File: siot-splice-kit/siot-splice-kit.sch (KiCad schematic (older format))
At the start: 2 parts, among them J1 xConnect_smd, J2 Screw_Terminal_5mm_01x03

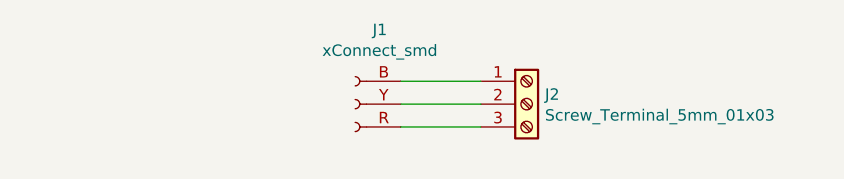
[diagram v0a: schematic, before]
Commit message: updates for relay/splice kit
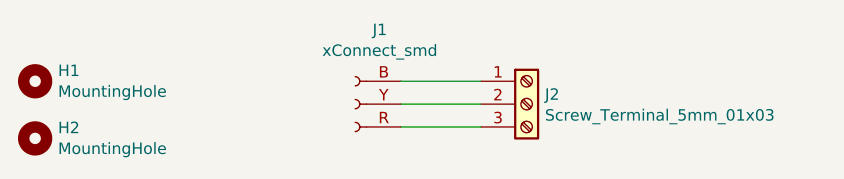
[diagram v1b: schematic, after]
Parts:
- added H1, H2: MountingHole, MountingHole:MountingHole_3.5mm, symbol Mechanical:MountingHole
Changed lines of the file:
@@
 EESchema Schematic File Version 4
+LIBS:siot-splice-kit-cache
 EELAYER 30 0
 EELAYER END
@@
 Wire Wire Line
 	4100 3350 4450 3350
+$Comp
+L Mechanical:MountingHole H1
+U 1 1 5DB9C90A
+P 2500 3150
+F 0 "H1" H 2600 3196 50  0000 L CNN
+F 1 "MountingHole" H 2600 3105 50  0000 L CNN
+F 2 "MountingHole:MountingHole_3.5mm" H 2500 3150 50  0001 C CNN
+F 3 "~" H 2500 3150 50  0001 C CNN
+	1    2500 3150
+	1    0    0    -1
+$EndComp
+$Comp
+L Mechanical:MountingHole H2
+U 1 1 5DB9C910
+P 2500 3400
+F 0 "H2" H 2600 3446 50  0000 L CNN
+F 1 "MountingHole" H 2600 3355 50  0000 L CNN
+F 2 "MountingHole:MountingHole_3.5mm" H 2500 3400 50  0001 C CNN
+F 3 "~" H 2500 3400 50  0001 C CNN
+	1    2500 3400
+	1    0    0    -1
+$EndComp
 $EndSCHEMATC
